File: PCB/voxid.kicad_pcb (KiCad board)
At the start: 2 copper layers, 117 x 72 mm, 49 parts, among them J1 Conn_01x02_Pin, J2 Conn_01x02_Pin, J3 Conn_01x02_Pin, J4 v3.3, J6 AudioOut, J7 Conn_01x02_Pin, U1 TL072, U2 TL072, U3 TL072, U4 LM1117T-3.3

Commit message: feat: Actualizar diseño PCB y agregar diagrama del sistema
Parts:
- added C2: 470nF, Capacitor_THT:CP_Radial_Tantal_D5.0mm_P5.00mm, F.Cu at (-74.2, 6.57)
- added C3: 470nF, Capacitor_THT:CP_Radial_Tantal_D5.0mm_P5.00mm, F.Cu at (-74.2, 15.1)
- added C4: 470nF, Capacitor_THT:CP_Radial_Tantal_D5.0mm_P5.00mm, F.Cu at (-74.2, 23.5)
- added C6: 27nF, Capacitor_THT:CP_Radial_Tantal_D5.0mm_P5.00mm, F.Cu at (-65.7, 6.57)
- added C7: 2.7nF, Capacitor_THT:CP_Radial_Tantal_D5.0mm_P5.00mm, F.Cu at (-65.7, 15.1)
- added C8: 27nF, Capacitor_THT:CP_Radial_Tantal_D5.0mm_P5.00mm, F.Cu at (-65.7, 23.5)
- added C9: 20nF, Capacitor_THT:CP_Radial_Tantal_D5.0mm_P5.00mm, F.Cu at (-57.2, 6.57)
- added Caudio1: 1uF, Capacitor_THT:CP_Radial_Tantal_D5.0mm_P5.00mm, F.Cu at (-57.2, 15.1)
- added Cref1: 10uF, Capacitor_THT:CP_Radial_Tantal_D5.0mm_P5.00mm, F.Cu at (-57.2, 23.5)
- added R1: 1.3k, Resistor_THT:R_Axial_DIN0411_L9.9mm_D3.6mm_P12.70mm_Horizontal, F.Cu at (-90.6, 4.89)
- added R10: 779, Resistor_THT:R_Axial_DIN0411_L9.9mm_D3.6mm_P12.70mm_Horizontal, F.Cu at (-90.6, 35.8)
- added R14: 1.67.k, Resistor_THT:R_Axial_DIN0411_L9.9mm_D3.6mm_P12.70mm_Horizontal, F.Cu at (-90.6, 40.9)
- added R15: 2.2k, Resistor_THT:R_Axial_DIN0411_L9.9mm_D3.6mm_P12.70mm_Horizontal, F.Cu at (-90.6, 46.1)
- added R16: 1k, Resistor_THT:R_Axial_DIN0411_L9.9mm_D3.6mm_P12.70mm_Horizontal, F.Cu at (-90.6, 51.2)
- added R17: 10k, Resistor_THT:R_Axial_DIN0411_L9.9mm_D3.6mm_P12.70mm_Horizontal, F.Cu at (-90.6, 56.4)
- added R18: 10k, Resistor_THT:R_Axial_DIN0411_L9.9mm_D3.6mm_P12.70mm_Horizontal, F.Cu at (-90.6, 61.5)
- added R19: 10k, Resistor_THT:R_Axial_DIN0411_L9.9mm_D3.6mm_P12.70mm_Horizontal, F.Cu at (-90.6, 66.7)
- added R2: 8.87k, Resistor_THT:R_Axial_DIN0411_L9.9mm_D3.6mm_P12.70mm_Horizontal, F.Cu at (-90.6, 10.0)
- added R20: 10k, Resistor_THT:R_Axial_DIN0411_L9.9mm_D3.6mm_P12.70mm_Horizontal, F.Cu at (-90.6, 71.8)
- added R21: 10k, Resistor_THT:R_Axial_DIN0411_L9.9mm_D3.6mm_P12.70mm_Horizontal, F.Cu at (-90.6, 77.0)
- added R3: 3.09k, Resistor_THT:R_Axial_DIN0411_L9.9mm_D3.6mm_P12.70mm_Horizontal, F.Cu at (-90.6, 15.2)
- added R4: 3.65k, Resistor_THT:R_Axial_DIN0411_L9.9mm_D3.6mm_P12.70mm_Horizontal, F.Cu at (-90.6, 20.3)
- added R5: 1.64k, Resistor_THT:R_Axial_DIN0411_L9.9mm_D3.6mm_P12.70mm_Horizontal, F.Cu at (-90.6, 25.5)
- added R6: 5.87k, Resistor_THT:R_Axial_DIN0411_L9.9mm_D3.6mm_P12.70mm_Horizontal, F.Cu at (-90.6, 30.6)
- C1: renamed from C6; value 100nF -> 470nF
- J1: renamed from J7; value Conn_01x02_Pin -> Audio
- J2: renamed from J3; value Conn_01x02_Pin -> HPF_O
- J3: renamed from J1; value Conn_01x02_Pin -> LPFO
- J4: renamed from J2; value Conn_01x02_Pin -> Offset
- R22: renamed from R5; footprint Resistor_THT:R_Axial_DIN0309_L9.0mm_D3.2mm_P12.70mm_Horizontal -> Resistor_THT:R_Axial_DIN0411_L9.9mm_D3.6mm_P12.70mm_Horizontal
- R23: renamed from R4; footprint Resistor_THT:R_Axial_DIN0309_L9.0mm_D3.2mm_P12.70mm_Horizontal -> Resistor_THT:R_Axial_DIN0411_L9.9mm_D3.6mm_P12.70mm_Horizontal
- renumbered C1 to Cin1, C10 to Cout1, J4 to J5, RV10 to RV1, RV9 to RV2, TP01 to TP1
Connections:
- net Net-(J7-Pin_1) renamed Sound
- C1 pad 2: Net-(C6-Pad2) -> Net-(C1-Pad2)
- J1 pad 2: Net-(J7-Pin_2) -> Net-(J1-Pin_2)
- J2 pad 1: Net-(J3-Pin_1) -> HPF
- J2 pad 2: Net-(J3-Pin_2) -> Net-(J2-Pin_2)
- J3 pad 1: Net-(J1-Pin_1) -> LPF
- J3 pad 2: Net-(J1-Pin_2) -> Net-(J3-Pin_2)
- J4 pad 2: Net-(J2-Pin_2) -> Net-(J4-Pin_2)
- RV1 pad 1: Net-(R13-Pad1) -> Net-(R17-Pad2)
- RV1 pad 2: Net-(R13-Pad1) -> Net-(R17-Pad2)
- RV1 pad 3: Net-(J7-Pin_2) -> Net-(J1-Pin_2)
- U1 pad 1: Net-(J7-Pin_2) -> Net-(J1-Pin_2)
- U2 pad 6: Net-(J3-Pin_2) -> Net-(J2-Pin_2)
- U2 pad 7: Net-(J3-Pin_2) -> Net-(J2-Pin_2)
- U3 pad 1: Net-(J1-Pin_2) -> Net-(J3-Pin_2)
- U3 pad 2: Net-(J1-Pin_2) -> Net-(J3-Pin_2)
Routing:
- net Net-(J1-Pin_2): track 13.8 -> 44.0 mm
- net Net-(J7-Pin_2): track 30.1 -> 0.00 mm

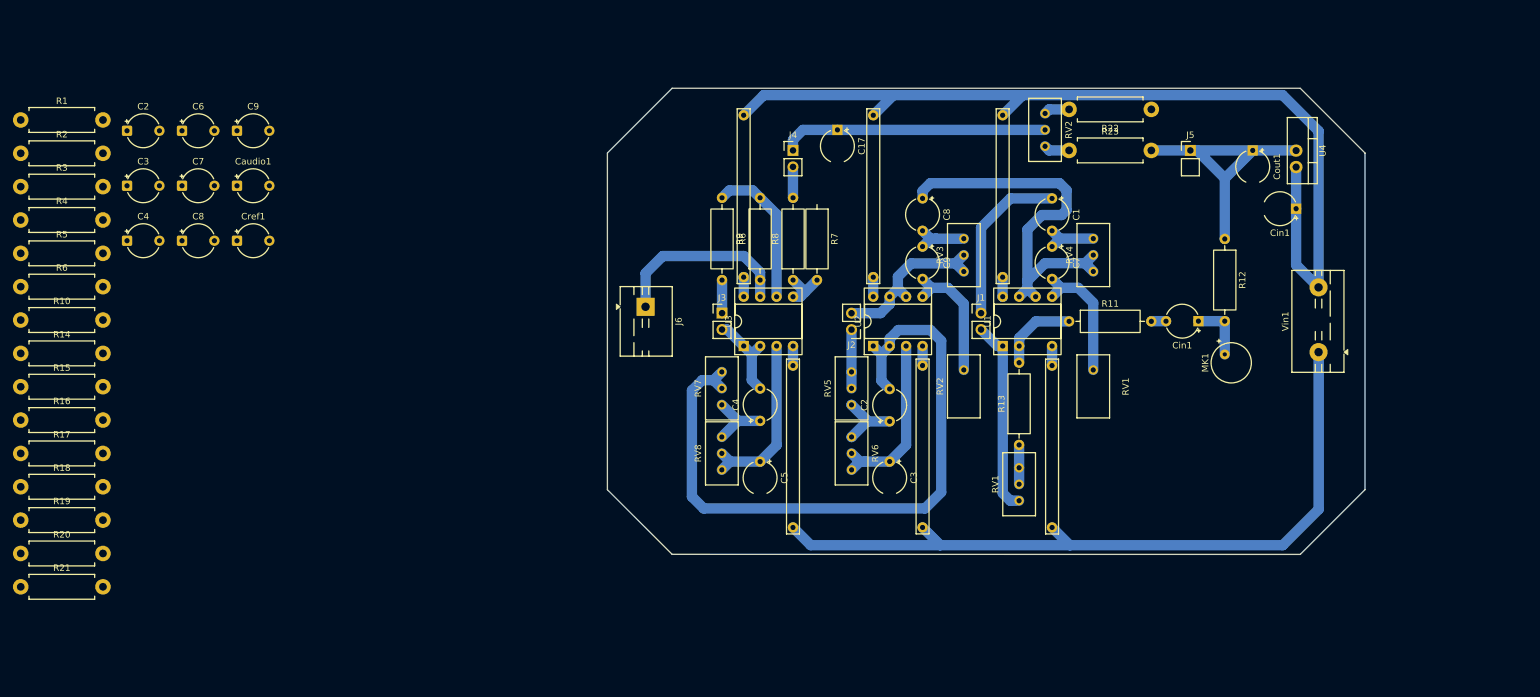
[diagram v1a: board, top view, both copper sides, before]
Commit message: pcb: Sustituir potenciometros por resistencias fijas comerciales
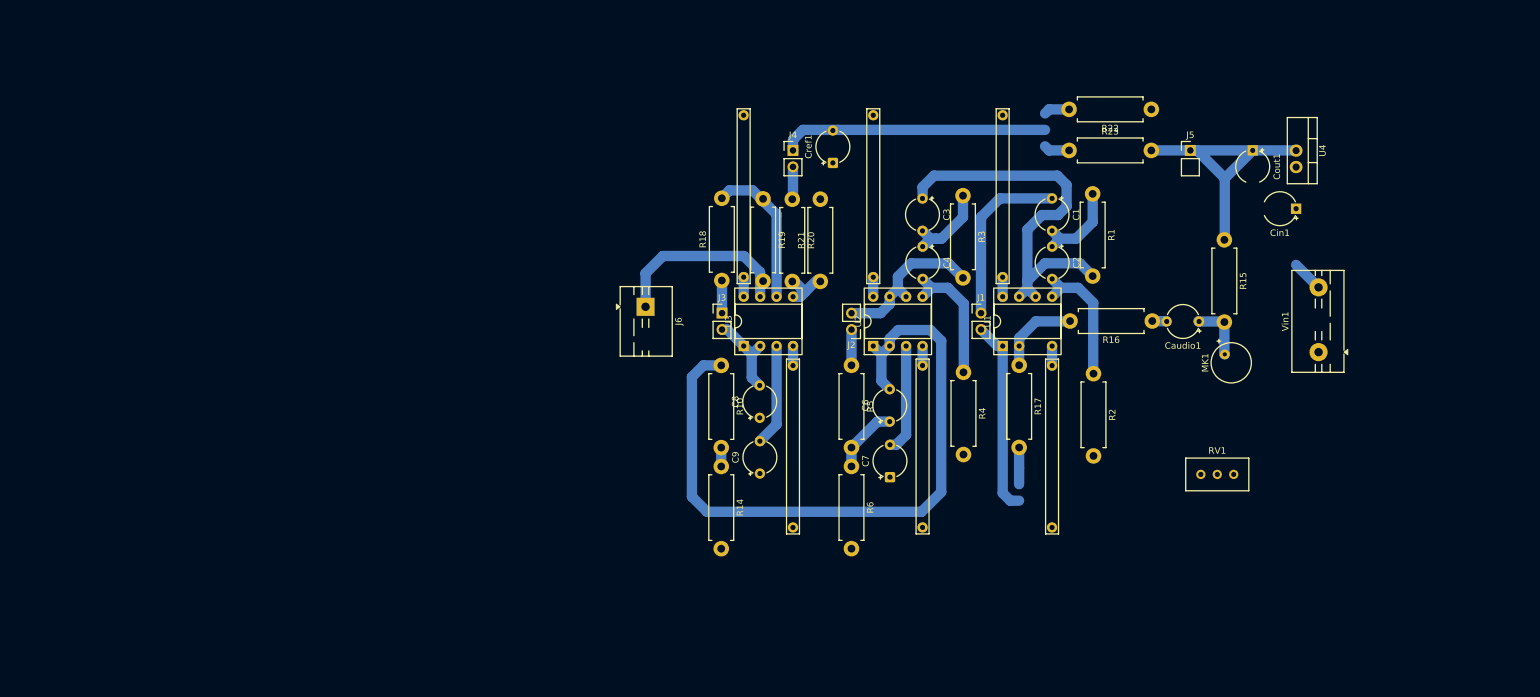
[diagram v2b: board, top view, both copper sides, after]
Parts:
- removed C17: 100nF, Capacitor_THT:CP_Radial_Tantal_D5.0mm_P5.00mm
- removed the C2 at (43.6, 51.5)
- removed the C3 at (43.6, 57.6)
- removed the C4 at (23.6, 51.4)
- removed C5: 10nF, Capacitor_THT:CP_Radial_Tantal_D5.0mm_P5.00mm
- removed the C7 at (68.7, 24.4)
- removed the C8 at (48.7, 17.0)
- removed the C9 at (48.7, 24.4)
- removed the Cin1 at (91.3, 36.0)
- removed R11: 1k, Resistor_THT:R_Axial_DIN0309_L9.0mm_D3.2mm_P12.70mm_Horizontal
- removed R12: 2.2k, Resistor_THT:R_Axial_DIN0309_L9.0mm_D3.2mm_P12.70mm_Horizontal
- removed R13, R7, R8, R9: 10k, Resistor_THT:R_Axial_DIN0309_L9.0mm_D3.2mm_P12.70mm_Horizontal
- removed the R6 at (23.6, 29.6)
- removed the RV1 at (75.0, 43.5)
- removed the RV1 at (63.6, 58.6)
- removed RV2: 100, Potentiometer_THT:Potentiometer_Bourns_3296W_Vertical
- removed RV2: 41.2k, Potentiometer_THT:Potentiometer_Bourns_3296W_Vertical
- removed RV3: 6.04k, Potentiometer_THT:Potentiometer_Bourns_3296W_Vertical
- removed RV4: 14.7k, Potentiometer_THT:Potentiometer_Bourns_3296W_Vertical
- removed RV5, RV6: 2.43k, Potentiometer_THT:Potentiometer_Bourns_3296W_Vertical
- removed RV7, RV8: 1.02k, Potentiometer_THT:Potentiometer_Bourns_3296W_Vertical
- added RV1: 100k, Potentiometer_THT:Potentiometer_Bourns_3296W_Vertical, F.Cu at (96.7, 59.6)
- Cout1: value 100nF -> 10uF
- Cref1: value 10uF -> 22uF
- R22: value 10k -> 1.05K
- R23: value 10k -> 1k
- moved R15 187.3 mm to (95.3, 23.4), turned to -90 degrees
- moved R16 175.4 mm to (84.2, 36.0), turned to 180 degrees
- moved R2 169.1 mm to (75.1, 44.1), turned to -90 degrees
- moved R1 165.9 mm to (74.9, 16.3), turned to -90 degrees
- moved R17 154.8 mm to (63.6, 42.8), turned to -90 degrees
- moved Caudio1 150.1 mm to (91.4, 36.0), turned to 180 degrees
- moved R4 147.5 mm to (55.0, 43.9), turned to -90 degrees
- moved R3 145.5 mm to (54.9, 16.6), turned to -90 degrees
- moved C2 144.0 mm to (68.7, 24.4), turned to -90 degrees
- moved R21 132.2 mm to (32.9, 29.8), turned to 90 degrees
- moved R6 131.3 mm to (37.7, 58.4), turned to -90 degrees
- moved R20 131.1 mm to (28.6, 17.1), turned to -90 degrees
- moved R5 129.5 mm to (37.7, 42.8), turned to -90 degrees
- moved R19 124.9 mm to (24.0, 17.1), turned to -90 degrees
- moved C4 122.9 mm to (48.7, 24.4), turned to -90 degrees
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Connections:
- R22 pad 2: Net-(R22-Pad2) -> Vref
- R23 pad 1: Net-(R23-Pad1) -> Vref
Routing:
- net +12V: track 154.4 -> 14.1 mm
- net -12V: track 125.6 -> 9.06 mm
- net Net-(J2-Pin_2): track 4.78 -> 24.9 mm
- net Net-(C1-Pad2): track 0.00 -> 13.9 mm
- net Net-(J1-Pin_2): track 44.0 -> 30.1 mm
- net Net-(J3-Pin_2): track 26.4 -> 13.3 mm
- net Net-(C3-Pad2): track 0.00 -> 12.9 mm
- net Net-(U3A-+): track 27.1 -> 15.8 mm
- net Net-(C2-Pad1): track 10.5 -> 0.00 mm
- net Net-(C6-Pad1): track 0.00 -> 10.5 mm
- net Net-(C4-Pad1): track 10.5 -> 0.00 mm
- net Net-(U2A-+): track 27.1 -> 16.8 mm
- net Net-(J3-Pin_1): track 9.08 -> 0.00 mm
- net Net-(C8-Pad2): track 8.61 -> 0.00 mm
- net Net-(C6-Pad2): track 8.60 -> 0.00 mm
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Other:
- board outline removed

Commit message: pcb: enrutado
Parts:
- added D1: 1N5819, Diode_THT:D_DO-41_SOD81_P10.16mm_Horizontal, F.Cu at (23.5, 13.0)
- added D2: 1N5819, Diode_THT:D_DO-41_SOD81_P10.16mm_Horizontal, F.Cu at (23.5, 30.0)
- added Rlim1: 4.7k, Resistor_THT:R_Axial_DIN0411_L9.9mm_D3.6mm_P12.70mm_Horizontal, F.Cu at (36.2, 26.6)
- C6, C8: value 27nF -> 22nF
- C7: value 2.7nF -> 2.2nF
- C9: value 20nF -> 10nF
- R1: value 1.3k -> 1.2k
- R10: value 779 -> 820
- R14: value 1.67.k -> 3.9k
- R2: value 8.87k -> 8.2k
- R3: value 3.09k -> 3.3k
- R4: value 3.65k -> 3.9k
- R5: value 1.64k -> 2.2k
- R6: value 5.87k -> 6.8k
- moved C9 26.9 mm to (48.3, 70.0)
- moved C7 26.7 mm to (68.4, 70.0)
- moved C8 25.5 mm to (48.4, 56.8)
- moved C6 25.4 mm to (68.4, 56.8)
- moved Caudio1 25.3 mm to (116.6, 35.8)
- moved Cout1 25.0 mm to (124.6, 8.34)
- moved U4 25.0 mm to (131.3, 5.87)
- moved Cin1 25.0 mm to (131.3, 18.5)
- moved R20 24.9 mm to (53.5, 16.4)
- moved R15 24.9 mm to (120.2, 23.1)
- moved R18 24.9 mm to (42.5, 29.1)
- moved J4 24.9 mm to (53.5, 10.6)
- moved J5 24.8 mm to (114.8, 8.35)
- moved TP2 24.8 mm to (45.9, 29.4)
- moved TP5 24.8 mm to (73.5, 42.7)
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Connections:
- J6 pad 1: Net-(J6-Pin_1) -> Net-(D1-A)
- R19 pad 2: Net-(J6-Pin_1) -> S
- U3 pad 7: Net-(J6-Pin_1) -> S
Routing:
- net Net-(J6-Pin_1): track 28.8 -> 0.00 mm
- net Vref: track 49.1 -> 24.0 mm
- net Net-(U2A--): track 107.7 -> 129.2 mm
- net Net-(U3A-+): track 15.8 -> 34.8 mm
- net Net-(U2A-+): track 16.8 -> 34.8 mm
- net Net-(D1-A): track 0.00 -> 17.8 mm
- net S: track 0.00 -> 16.9 mm
- net Net-(J2-Pin_2): track 24.9 -> 13.1 mm
- net Net-(C3-Pad2): track 12.9 -> 2.45 mm
- net Net-(J3-Pin_2): track 13.3 -> 19.4 mm
- net Net-(MK1-+): track 9.30 -> 3.53 mm
- net Net-(C8-Pad1): track 2.91 -> 8.64 mm
- net +3.3V: track 43.9 -> 39.5 mm
- net Net-(U3B-+): track 7.38 -> 11.1 mm
- net Net-(C6-Pad1): track 10.5 -> 8.59 mm
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
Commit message: pcb: Creacion de geber para cnc
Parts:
- added Cref2: 100nF, Capacitor_THT:CP_Radial_Tantal_D5.0mm_P5.00mm, F.Cu at (91.7, 87.4)
- added Cref3: 100nF, Capacitor_THT:CP_Radial_Tantal_D5.0mm_P5.00mm, F.Cu at (71.7, 82.4)
- added Cref4: 100nF, Capacitor_THT:CP_Radial_Tantal_D5.0mm_P5.00mm, F.Cu at (44.1, 3.46)
- added Cref5: 100nF, Capacitor_THT:CP_Radial_Tantal_D5.0mm_P5.00mm, F.Cu at (64.1, 8.46)
- added Cref6: 100nF, Capacitor_THT:CP_Radial_Tantal_D5.0mm_P5.00mm, F.Cu at (84.0, 3.46)
- added Cref7: 100nF, Capacitor_THT:CP_Radial_Tantal_D5.0mm_P5.00mm, F.Cu at (51.7, 87.4)
- added J7: v3.3, Connector_PinHeader_2.54mm:PinHeader_1x02_P2.54mm_Vertical, F.Cu at (12.1, 36.7)
- moved R10 38.5 mm to (44.2, 81.1), turned to 90 degrees
- moved J5 15.1 mm to (101.0, 14.4)
- moved C9 14.8 mm to (35.4, 62.9), turned to 0 degrees
- moved R23 13.9 mm to (62.8, 14.4)
- moved R22 13.9 mm to (75.5, 18.5)
- moved C8 13.0 mm to (35.4, 55.3), turned to 0 degrees
- moved C6 12.1 mm to (61.7, 66.9)
- moved R18 12.1 mm to (35.8, 39.2)
- moved R5 12.1 mm to (55.8, 52.8)
- moved TP1 12.1 mm to (79.1, 39.5)
- moved TP2 12.1 mm to (39.1, 39.5)
- moved TP3 12.1 mm to (59.1, 39.5)
- moved D1 12.1 mm to (16.8, 23.1)
- moved C1 12.1 mm to (86.8, 27.0)
- moved C3 12.1 mm to (66.8, 27.0)
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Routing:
- net +12V: track 15.5 -> 175.1 mm
- net -12V: track 9.06 -> 137.6 mm
- net +3.3V: track 39.5 -> 150.1 mm
- net Net-(U2A--): track 129.2 -> 51.7 mm
- net Net-(U3A-+): track 34.8 -> 14.7 mm
- net Net-(C8-Pad1): track 8.64 -> 23.9 mm
- net Net-(C3-Pad2): track 2.45 -> 11.5 mm
- net Net-(J3-Pin_2): track 19.4 -> 12.3 mm
- net Net-(MK1-+): track 3.53 -> 8.71 mm
- net Net-(U2B-+): track 20.5 -> 19.4 mm
- net Vref: track 24.0 -> 23.2 mm
- net Net-(U1B-+): track 20.2 -> 19.5 mm
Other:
- board outline added: 142 x 92 mm

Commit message: pcb: Pcb lista :)
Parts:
- added J8: Offset, Connector_PinHeader_2.54mm:PinHeader_1x02_P2.54mm_Vertical, F.Cu at (20.1, 19.9)
- R1, R10, R14, R15, R16, R17, R18, R19, R2, R20, R21, R22, R23, R3, R4, R5, R6, Rlim1: footprint Resistor_THT:R_Axial_DIN0411_L9.9mm_D3.6mm_P12.70mm_Horizontal -> Resistor_THT:R_Axial_DIN0207_L6.3mm_D2.5mm_P7.62mm_Horizontal
- moved J5 18.5 mm to (82.7, 17.4)
- moved C7 17.0 mm to (73.2, 57.5), turned to 90 degrees
- moved C9 13.8 mm to (48.0, 57.5), turned to 90 degrees
- moved R4 13.2 mm to (73.9, 39.6), turned to 90 degrees
- moved R10 11.7 mm to (41.3, 69.7)
- moved C6 9.38 mm to (62.4, 57.5)
- moved RV1 9.15 mm to (88.7, 63.5)
- moved R23 9.00 mm to (71.3, 17.4)
- moved R1 8.88 mm to (100.0, 31.8)
- moved Vin1 8.04 mm to (125.0, 50.8)
- moved Cref6 7.55 mm to (90.7, 7.05)
- moved R17 7.06 mm to (88.7, 52.4)
- moved C1 7.05 mm to (93.8, 27.0)
- moved J1 7.05 mm to (82.8, 44.7)
- moved R2 7.05 mm to (100.2, 52.8)
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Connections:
- D1 pad 1: +3.3V -> Net-(D1-K)
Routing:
- net +12V: track 175.1 -> 147.8 mm
- net +3.3V: track 150.1 -> 127.7 mm
- net Net-(U2A--): track 51.7 -> 34.4 mm
- net Net-(C8-Pad1): track 23.9 -> 8.47 mm
- net Vref: track 23.2 -> 35.6 mm
- net Net-(U2B-+): track 19.4 -> 8.13 mm
- net Net-(MK1-+): track 8.71 -> 16.1 mm
- net Net-(J2-Pin_2): track 13.1 -> 20.2 mm
- net Net-(U2A-+): track 34.8 -> 41.5 mm
- net Net-(U1B--): track 60.9 -> 67.5 mm
- net Net-(C6-Pad1): track 8.59 -> 2.10 mm
- net Net-(J1-Pin_2): track 30.8 -> 24.9 mm
- net -12V: track 137.6 -> 132.2 mm
- net Net-(U3B--): track 23.8 -> 18.5 mm
- net Net-(C1-Pad2): track 13.9 -> 9.02 mm
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
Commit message: pcb: ahora si, pcb lista e imagen de la pcb agregada a DOC
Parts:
- removed R22: 1.05K, Resistor_THT:R_Axial_DIN0207_L6.3mm_D2.5mm_P7.62mm_Horizontal
- added RV2: 1.05k, Potentiometer_THT:Potentiometer_Bourns_3296W_Vertical, F.Cu at (77.5, 21.0)
- moved R23 0.54 mm to (71.2, 16.9)
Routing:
- net GND: track 0.00 -> 404.9 mm
- net Net-(U1B--): track 67.5 -> 64.9 mm
- net Vref: track 35.6 -> 37.7 mm
- net +3.3V: track 127.7 -> 128.2 mm
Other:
- board size 142 x 92 mm -> 130 x 90 mm

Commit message: pcb: Esta es la pcb buena :c
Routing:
- net +12V: track 147.8 -> 162.6 mm
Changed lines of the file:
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@@
+	)
+	(segment
+		(start 120.890372 27.55845)
+		(end 120.890372 36.672872)
+		(width 1.6)
+		(layer "B.Cu")
+		(net "+12V")
 	)
 	(segment
@@
 		(width 1.6)
 		(layer "B.Cu")
+		(net "+12V")
+	)
+	(segment
+		(start 120.890372 36.672872)
+		(end 124.9675 40.75)
+		(width 1.6)
+		(layer "B.Cu")
